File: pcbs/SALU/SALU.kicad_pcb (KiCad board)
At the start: 4 copper layers, 99 parts, among them J201 Conn_02x20_Odd_Even, U201 74HC245, U202 74HC245, U301 74HC138, U302 74HC138, U401 74HC245, U402 74HC86, U403 74HC08, U404 74HC283, U405 74HC283, U406 74HC245, U407 74HC245, U501 74HC00, U502 74HC00, U503 74HC245, U504 74HC245, U601 74HC245, U602 74HC245, U701 74HC08, U702 74HCT125, U703 74HC245, U704 74HC245

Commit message: More routing
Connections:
- U406 pad 11: /Incrementer-Decrementer/RESULT7 -> /Barrel Shifters/RESULT7
- U406 pad 12: /Incrementer-Decrementer/RESULT6 -> /Barrel Shifters/RESULT6
- U406 pad 13: /Incrementer-Decrementer/RESULT5 -> /Barrel Shifters/RESULT5
- U406 pad 14: /Incrementer-Decrementer/RESULT4 -> /Barrel Shifters/RESULT4
- U406 pad 15: /Incrementer-Decrementer/RESULT3 -> /Barrel Shifters/RESULT3
- U406 pad 16: /Incrementer-Decrementer/RESULT2 -> /Barrel Shifters/RESULT2
- U406 pad 17: /Incrementer-Decrementer/RESULT1 -> /Barrel Shifters/RESULT1
- U406 pad 18: /Incrementer-Decrementer/RESULT0 -> /Barrel Shifters/RESULT0
- U503 pad 11: /Incrementer-Decrementer/RESULT7 -> /Barrel Shifters/RESULT7
- U503 pad 12: /Incrementer-Decrementer/RESULT6 -> /Barrel Shifters/RESULT6
- U503 pad 13: /Incrementer-Decrementer/RESULT5 -> /Barrel Shifters/RESULT5
- U503 pad 14: /Incrementer-Decrementer/RESULT4 -> /Barrel Shifters/RESULT4
- U503 pad 15: /Incrementer-Decrementer/RESULT3 -> /Barrel Shifters/RESULT3
- U503 pad 16: /Incrementer-Decrementer/RESULT2 -> /Barrel Shifters/RESULT2
- U503 pad 17: /Incrementer-Decrementer/RESULT1 -> /Barrel Shifters/RESULT1
- U503 pad 18: /Incrementer-Decrementer/RESULT0 -> /Barrel Shifters/RESULT0
- U504 pad 11: /Incrementer-Decrementer/RESULT7 -> /Barrel Shifters/RESULT7
- U504 pad 12: /Incrementer-Decrementer/RESULT6 -> /Barrel Shifters/RESULT6
- U504 pad 13: /Incrementer-Decrementer/RESULT5 -> /Barrel Shifters/RESULT5
- U504 pad 14: /Incrementer-Decrementer/RESULT4 -> /Barrel Shifters/RESULT4
- U504 pad 15: /Incrementer-Decrementer/RESULT3 -> /Barrel Shifters/RESULT3
- U504 pad 16: /Incrementer-Decrementer/RESULT2 -> /Barrel Shifters/RESULT2
- U504 pad 17: /Incrementer-Decrementer/RESULT1 -> /Barrel Shifters/RESULT1
- U504 pad 18: /Incrementer-Decrementer/RESULT0 -> /Barrel Shifters/RESULT0
- U703 pad 11: /Shifters/RESULT7 -> /Barrel Shifters/RESULT7
- U703 pad 12: /Shifters/RESULT6 -> /Barrel Shifters/RESULT6
- U703 pad 13: /Shifters/RESULT5 -> /Barrel Shifters/RESULT5
- U703 pad 14: /Shifters/RESULT4 -> /Barrel Shifters/RESULT4
- U703 pad 15: /Shifters/RESULT3 -> /Barrel Shifters/RESULT3
- U703 pad 16: /Shifters/RESULT2 -> /Barrel Shifters/RESULT2
- U703 pad 17: /Shifters/RESULT1 -> /Barrel Shifters/RESULT1
- U703 pad 18: /Shifters/RESULT0 -> /Barrel Shifters/RESULT0
- U704 pad 11: /Shifters/RESULT7 -> /Barrel Shifters/RESULT7
- U704 pad 12: /Shifters/RESULT6 -> /Barrel Shifters/RESULT6
- U704 pad 13: /Shifters/RESULT5 -> /Barrel Shifters/RESULT5
- U704 pad 14: /Shifters/RESULT4 -> /Barrel Shifters/RESULT4
- U704 pad 15: /Shifters/RESULT3 -> /Barrel Shifters/RESULT3
- U704 pad 16: /Shifters/RESULT2 -> /Barrel Shifters/RESULT2
- U704 pad 17: /Shifters/RESULT1 -> /Barrel Shifters/RESULT1
- U704 pad 18: /Shifters/RESULT0 -> /Barrel Shifters/RESULT0
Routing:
- net /Barrel Shifters/RESULT6: track 0.00 -> 225.4 mm, vias 0 -> 9
- net /Barrel Shifters/RESULT7: track 0.00 -> 224.9 mm, vias 0 -> 9
- net /Barrel Shifters/RESULT5: track 0.00 -> 215.8 mm, vias 0 -> 9
- net /Barrel Shifters/RESULT4: track 0.00 -> 215.5 mm, vias 0 -> 9
- net /Barrel Shifters/RESULT3: track 0.00 -> 215.2 mm, vias 0 -> 9
- net /Barrel Shifters/RESULT2: track 0.00 -> 215.0 mm, vias 0 -> 9
- net /Barrel Shifters/RESULT1: track 0.00 -> 214.0 mm, vias 0 -> 9
- net /Barrel Shifters/RESULT0: track 0.00 -> 213.7 mm, vias 0 -> 9
- net /Incrementer-Decrementer/RESULT0: track 137.8 -> 0.00 mm, vias 4 -> 0
- net /Incrementer-Decrementer/RESULT1: track 135.0 -> 0.00 mm, vias 4 -> 0
- net /Incrementer-Decrementer/RESULT2: track 132.9 -> 0.00 mm, vias 4 -> 0
- net /Incrementer-Decrementer/RESULT6: track 131.2 -> 0.00 mm, vias 4 -> 0
- net /Incrementer-Decrementer/RESULT3: track 130.1 -> 0.00 mm, vias 4 -> 0
- net /Incrementer-Decrementer/RESULT7: track 127.6 -> 0.00 mm, vias 4 -> 0
- net /Incrementer-Decrementer/RESULT4: track 127.3 -> 0.00 mm, vias 4 -> 0
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
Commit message: Fiddling around with shifters
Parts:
- moved C703 22.2 mm to (138.4, 47.0)
- moved C704 20.4 mm to (138.4, 62.2)
- moved C702 11.4 mm to (148.6, 22.9)
- moved U702 11.4 mm to (141.0, 26.7)
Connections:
- U701 pad 1: /Shifters/~{LSHIFT0} -> GND
- U701 pad 10: GND -> /Shifters/~{LSHIFT1}
- U701 pad 2: /Shifters/~{LSHIFT1} -> GND
- U701 pad 3: Net-(U701-Pad3) -> unconnected-(U701-Pad3)
- U701 pad 8: unconnected-(U701-Pad8) -> Net-(U703-Pad19)
- U701 pad 9: GND -> /Shifters/~{LSHIFT0}
- U702 pad 1: /Shifters/~{LSHIFT0} -> /Shifters/~{RSHIFT1}
- U702 pad 10: /Shifters/~{RSHIFT0} -> /Shifters/~{LSHIFT0}
- U702 pad 12: /Barrel Shifters/A0 -> /Barrel Shifters/A7
- U702 pad 13: /Shifters/~{RSHIFT1} -> /Shifters/~{LSHIFT1}
- U702 pad 2: /Barrel Shifters/A7 -> /Barrel Shifters/A0
- U702 pad 4: /Shifters/~{LSHIFT1} -> /Shifters/~{RSHIFT0}
- U702 pad 5: /Barrel Shifters/A7 -> /Barrel Shifters/A0
- U702 pad 9: /Barrel Shifters/A0 -> /Barrel Shifters/A7
- U703 pad 19: Net-(U701-Pad3) -> Net-(U703-Pad19)
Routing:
- net /Shifters/~{RSHIFT0}: track 0.00 -> 78.7 mm, vias 0 -> 2
- net /Shifters/~{LSHIFT0}: track 0.00 -> 72.4 mm, vias 0 -> 2
- net /Barrel Shifters/A7: track 253.8 -> 322.9 mm
- net Net-(U701-Pad6): track 0.00 -> 50.1 mm, vias 0 -> 2
- net /Barrel Shifters/A0: track 287.7 -> 325.9 mm
- net /Shifters/~{RSHIFT1}: track 0.00 -> 35.5 mm
- net /Shifters/FLAG: track 0.00 -> 31.6 mm
- net /Shifters/~{LSHIFT1}: track 0.00 -> 31.1 mm, vias 0 -> 1
- net Net-(U703-Pad19): track 0.00 -> 2.67 mm, vias 0 -> 1

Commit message: Working on output stage
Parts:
- added C801: 100n, Capacitor_SMD:C_0603_1608Metric, F.Cu at (174.0, 35.6)
- added C802: 100n, Capacitor_SMD:C_0603_1608Metric, F.Cu at (174.0, 58.4)
- added C803: 100n, Capacitor_SMD:C_0603_1608Metric, F.Cu at (157.5, 66.3)
- added C804: 100n, Capacitor_SMD:C_0603_1608Metric, F.Cu at (174.0, 82.5)
- added D801: GREEN, LED_SMD:LED_0603_1608Metric, F.Cu at (159.0, 85.1)
- added D802: GREEN, LED_SMD:LED_0603_1608Metric, F.Cu at (159.0, 87.6)
- added D803: GREEN, LED_SMD:LED_0603_1608Metric, F.Cu at (159.0, 90.2)
- added D804: GREEN, LED_SMD:LED_0603_1608Metric, F.Cu at (159.0, 92.7)
- added D805: GREEN, LED_SMD:LED_0603_1608Metric, F.Cu at (159.0, 95.2)
- added D806: GREEN, LED_SMD:LED_0603_1608Metric, F.Cu at (159.0, 97.8)
- added D807: GREEN, LED_SMD:LED_0603_1608Metric, F.Cu at (159.0, 100.3)
- added D808: GREEN, LED_SMD:LED_0603_1608Metric, F.Cu at (159.0, 102.9)
- added R801: 220k, Resistor_SMD:R_0603_1608Metric, F.Cu at (135.9, 81.1)
- added R802: 220k, Resistor_SMD:R_0603_1608Metric, F.Cu at (137.2, 77.3)
- added R803: 220k, Resistor_SMD:R_0603_1608Metric, F.Cu at (138.4, 81.1)
- added R804: 220k, Resistor_SMD:R_0603_1608Metric, F.Cu at (139.7, 77.3)
- added R805: 220k, Resistor_SMD:R_0603_1608Metric, F.Cu at (141.0, 81.1)
- added R806: 220k, Resistor_SMD:R_0603_1608Metric, F.Cu at (142.2, 77.3)
- added R807: 220k, Resistor_SMD:R_0603_1608Metric, F.Cu at (143.5, 81.1)
- added R808: 220k, Resistor_SMD:R_0603_1608Metric, F.Cu at (144.8, 77.3)
- added R809: 4k7, Resistor_SMD:R_0603_1608Metric, F.Cu at (155.2, 85.1)
- added R810: 4k7, Resistor_SMD:R_0603_1608Metric, F.Cu at (155.2, 87.6)
- added R811: 4k7, Resistor_SMD:R_0603_1608Metric, F.Cu at (155.2, 90.2)
- added R812: 4k7, Resistor_SMD:R_0603_1608Metric, F.Cu at (155.2, 92.7)
- added R813: 4k7, Resistor_SMD:R_0603_1608Metric, F.Cu at (155.2, 95.2)
- added R814: 4k7, Resistor_SMD:R_0603_1608Metric, F.Cu at (155.2, 97.8)
- added R815: 4k7, Resistor_SMD:R_0603_1608Metric, F.Cu at (155.2, 100.3)
- added R816: 4k7, Resistor_SMD:R_0603_1608Metric, F.Cu at (155.2, 102.9)
- added R817: 10k, Resistor_THT:R_Axial_DIN0207_L6.3mm_D2.5mm_P7.62mm_Horizontal, F.Cu at (157.5, 38.1)
- added U801: 74HC74, Package_DIP:DIP-14_W7.62mm_Socket, F.Cu at (162.6, 35.6)
- added U802: 74HC32, Package_DIP:DIP-14_W7.62mm_Socket, F.Cu at (162.6, 58.4)
- added U803: 74HC14, Package_SO:SOIC-14_3.9x8.7mm_P1.27mm, F.Cu at (154.9, 72.6)
- added U804: 74HCT574, Package_DIP:DIP-20_W7.62mm_Socket, F.Cu at (162.6, 82.5)
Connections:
- U702 pad 11: /Shifters/FLAG -> /Incrementer-Decrementer/FLAG
- U702 pad 3: /Shifters/FLAG -> /Incrementer-Decrementer/FLAG
- U702 pad 6: /Shifters/FLAG -> /Incrementer-Decrementer/FLAG
- U702 pad 8: /Shifters/FLAG -> /Incrementer-Decrementer/FLAG
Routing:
- net /Incrementer-Decrementer/FLAG: track 0.00 -> 94.4 mm, vias 0 -> 1
- net /Output Stage/EXECUTE: track 0.00 -> 80.4 mm
- net /Barrel Shifters/RESULT5: track 215.8 -> 262.9 mm, vias 9 -> 10
- net /Barrel Shifters/RESULT7: track 224.9 -> 267.7 mm, vias 9 -> 10
- net /Barrel Shifters/RESULT3: track 215.2 -> 257.5 mm, vias 9 -> 10
- net /Barrel Shifters/RESULT4: track 215.5 -> 256.5 mm, vias 9 -> 10
- net /Barrel Shifters/RESULT1: track 214.0 -> 252.5 mm, vias 9 -> 10
- net /Barrel Shifters/RESULT6: track 225.4 -> 261.9 mm, vias 9 -> 10
- net /Barrel Shifters/RESULT2: track 215.0 -> 251.2 mm, vias 9 -> 10
- net /Barrel Shifters/RESULT0: track 213.7 -> 246.8 mm, vias 9 -> 10
- net /Shifters/FLAG: track 31.6 -> 0.00 mm
- net /Output Stage/~{OE}: track 0.00 -> 16.0 mm
- net Net-(U802-Pad6): track 0.00 -> 5.88 mm
- net Net-(U802-Pad3): track 0.00 -> 2.54 mm
- net Net-(D807-Pad1): track 0.00 -> 2.20 mm
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
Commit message: Routing
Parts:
- moved J201 14.2 mm to (38.1, 64.8)
- moved R309 1.52 mm to (73.7, 132.1)
- moved D305 1.27 mm to (69.8, 142.2)
- moved D307 1.27 mm to (69.8, 137.2)
- moved D308 1.27 mm to (69.8, 139.7)
- moved D309 1.27 mm to (69.8, 127.0)
- moved D310 1.27 mm to (69.8, 129.5)
- moved D311 1.27 mm to (69.8, 132.1)
- moved D312 1.27 mm to (69.8, 134.6)
- moved D313 1.27 mm to (69.8, 168.9)
- moved D315 1.27 mm to (69.8, 153.7)
- moved D316 1.27 mm to (69.8, 156.2)
- moved D317 1.27 mm to (69.8, 158.8)
- moved D318 1.27 mm to (69.8, 161.3)
- moved D319 1.27 mm to (69.8, 163.8)
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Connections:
- J201 pad 19: /Connector/DALUFLAG -> /Connector/SALUFLAG
- U401 pad 19: /Incrementer-Decrementer/~{INC} -> /Instruction Decoder/~{INC}
- U402 pad 4: /Incrementer-Decrementer/~{INC} -> /Instruction Decoder/~{INC}
- U403 pad 1: /Incrementer-Decrementer/~{INC} -> /Instruction Decoder/~{INC}
- U403 pad 2: /Incrementer-Decrementer/~{DEC} -> /Instruction Decoder/~{DEC}
- U404 pad 7: /Incrementer-Decrementer/~{INC} -> /Instruction Decoder/~{INC}
- U503 pad 19: /Not-Copy/~{NOT} -> /Instruction Decoder/~{NOT}
- U504 pad 19: /Not-Copy/~{COPY} -> /Instruction Decoder/~{COPY}
- U601 pad 19: /Barrel Shifters/~{LBARREL} -> /Instruction Decoder/~{LBARREL}
- U602 pad 19: /Barrel Shifters/~{RBARREL} -> /Instruction Decoder/~{RBARREL}
- U701 pad 10: /Shifters/~{LSHIFT1} -> /Instruction Decoder/~{LSHIFT1}
- U701 pad 4: /Shifters/~{RSHIFT0} -> /Instruction Decoder/~{RSHIFT0}
- U701 pad 5: /Shifters/~{RSHIFT1} -> /Instruction Decoder/~{RSHIFT1}
- U701 pad 9: /Shifters/~{LSHIFT0} -> /Instruction Decoder/~{LSHIFT0}
- U702 pad 1: /Shifters/~{RSHIFT1} -> /Instruction Decoder/~{RSHIFT1}
- U702 pad 10: /Shifters/~{LSHIFT0} -> /Instruction Decoder/~{LSHIFT0}
- U702 pad 13: /Shifters/~{LSHIFT1} -> /Instruction Decoder/~{LSHIFT1}
- U702 pad 4: /Shifters/~{RSHIFT0} -> /Instruction Decoder/~{RSHIFT0}
- U703 pad 2: /Shifters/~{LSHIFT0} -> /Instruction Decoder/~{LSHIFT0}
- U704 pad 9: /Shifters/~{RSHIFT0} -> /Instruction Decoder/~{RSHIFT0}
- U801 pad 5: /Output Stage/SALUFLAG -> /Connector/SALUFLAG
- U804 pad 12: /Output Stage/C7 -> /Connector/C7
- U804 pad 13: /Output Stage/C6 -> /Connector/C6
- U804 pad 14: /Output Stage/C5 -> /Connector/C5
- U804 pad 15: /Output Stage/C4 -> /Connector/C4
- U804 pad 16: /Output Stage/C3 -> /Connector/C3
- U804 pad 17: /Output Stage/C2 -> /Connector/C2
- U804 pad 18: /Output Stage/C1 -> /Connector/C1
- U804 pad 19: /Output Stage/C0 -> /Connector/C0
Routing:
- net /Connector/C7: track 0.00 -> 196.6 mm
- net /Connector/C6: track 0.00 -> 192.5 mm
- net /Connector/C5: track 0.00 -> 188.4 mm
- net /Connector/C4: track 0.00 -> 184.4 mm
- net /Instruction Decoder/~{LSHIFT1}: track 0.00 -> 182.8 mm, vias 0 -> 1
- net /Connector/C3: track 0.00 -> 180.3 mm
- net /Instruction Decoder/~{RSHIFT0}: track 0.00 -> 178.0 mm, vias 0 -> 2
- net /Connector/C2: track 0.00 -> 176.2 mm
- net /Connector/C1: track 0.00 -> 172.2 mm
- net /Instruction Decoder/~{LSHIFT0}: track 0.00 -> 171.2 mm, vias 0 -> 4
- net /Connector/C0: track 0.00 -> 168.1 mm
- net /Instruction Decoder/~{RSHIFT1}: track 0.00 -> 146.0 mm, vias 0 -> 1
- net /Connector/SALUFLAG: track 0.00 -> 145.7 mm
- net /Instruction Decoder/~{DEC}: track 0.00 -> 114.8 mm
- net /Instruction Decoder/~{INC}: track 0.00 -> 99.9 mm, vias 0 -> 2
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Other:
- board text added: "RGE2023"

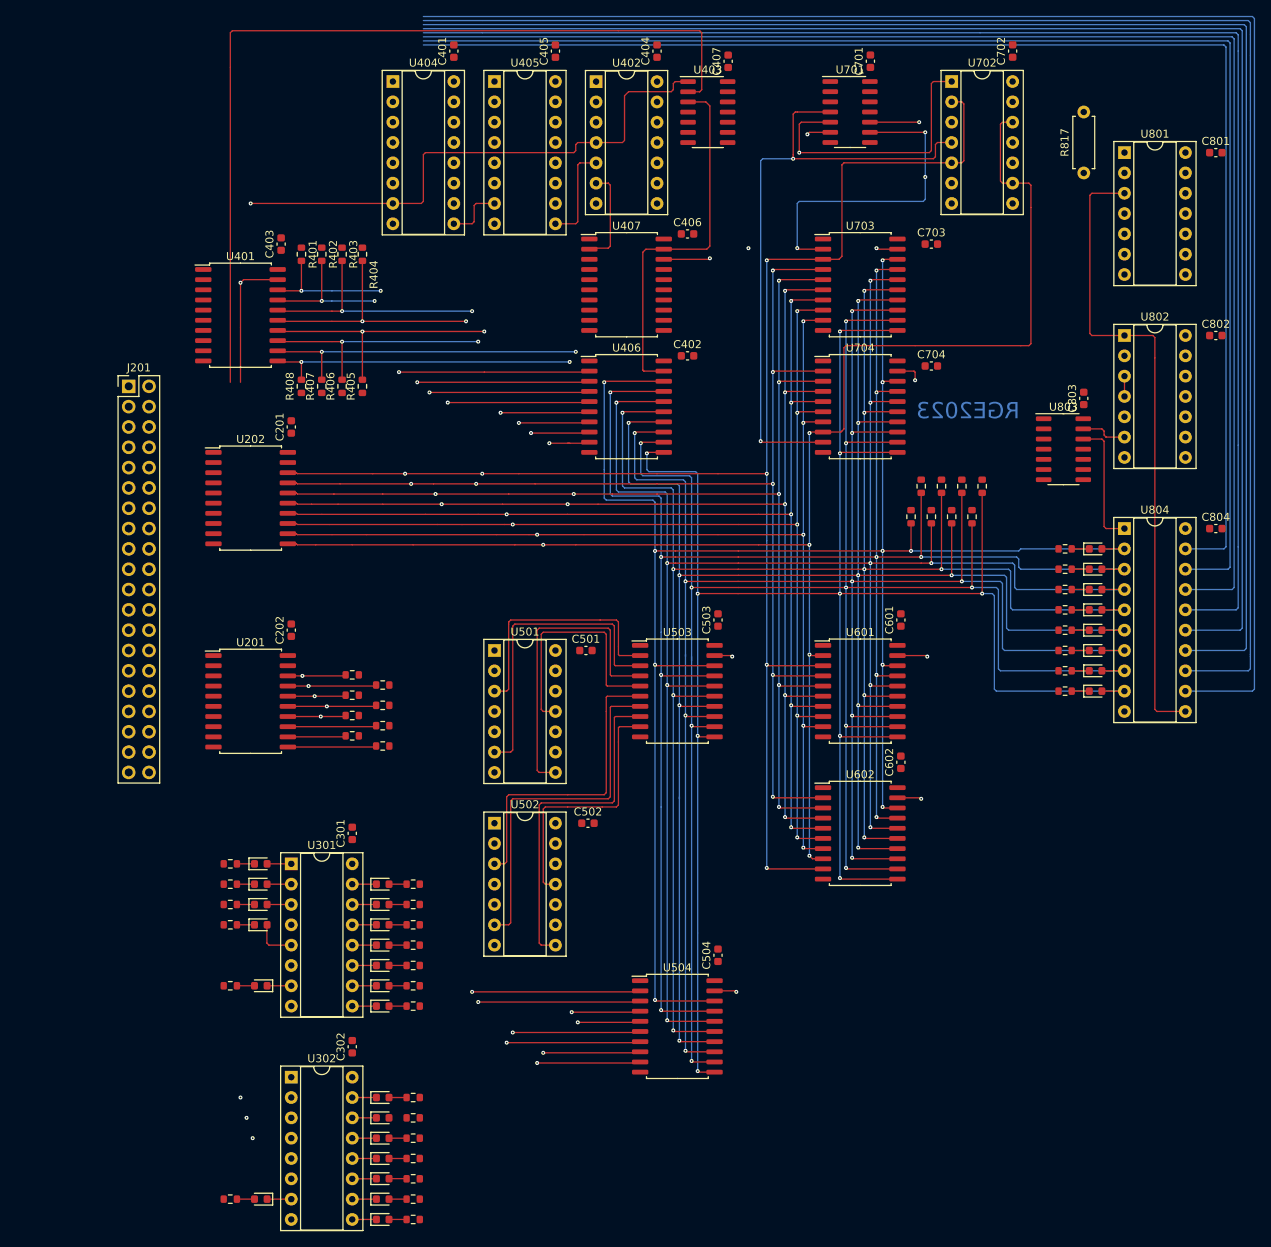
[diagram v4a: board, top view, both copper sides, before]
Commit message: Rethink position of second decoder
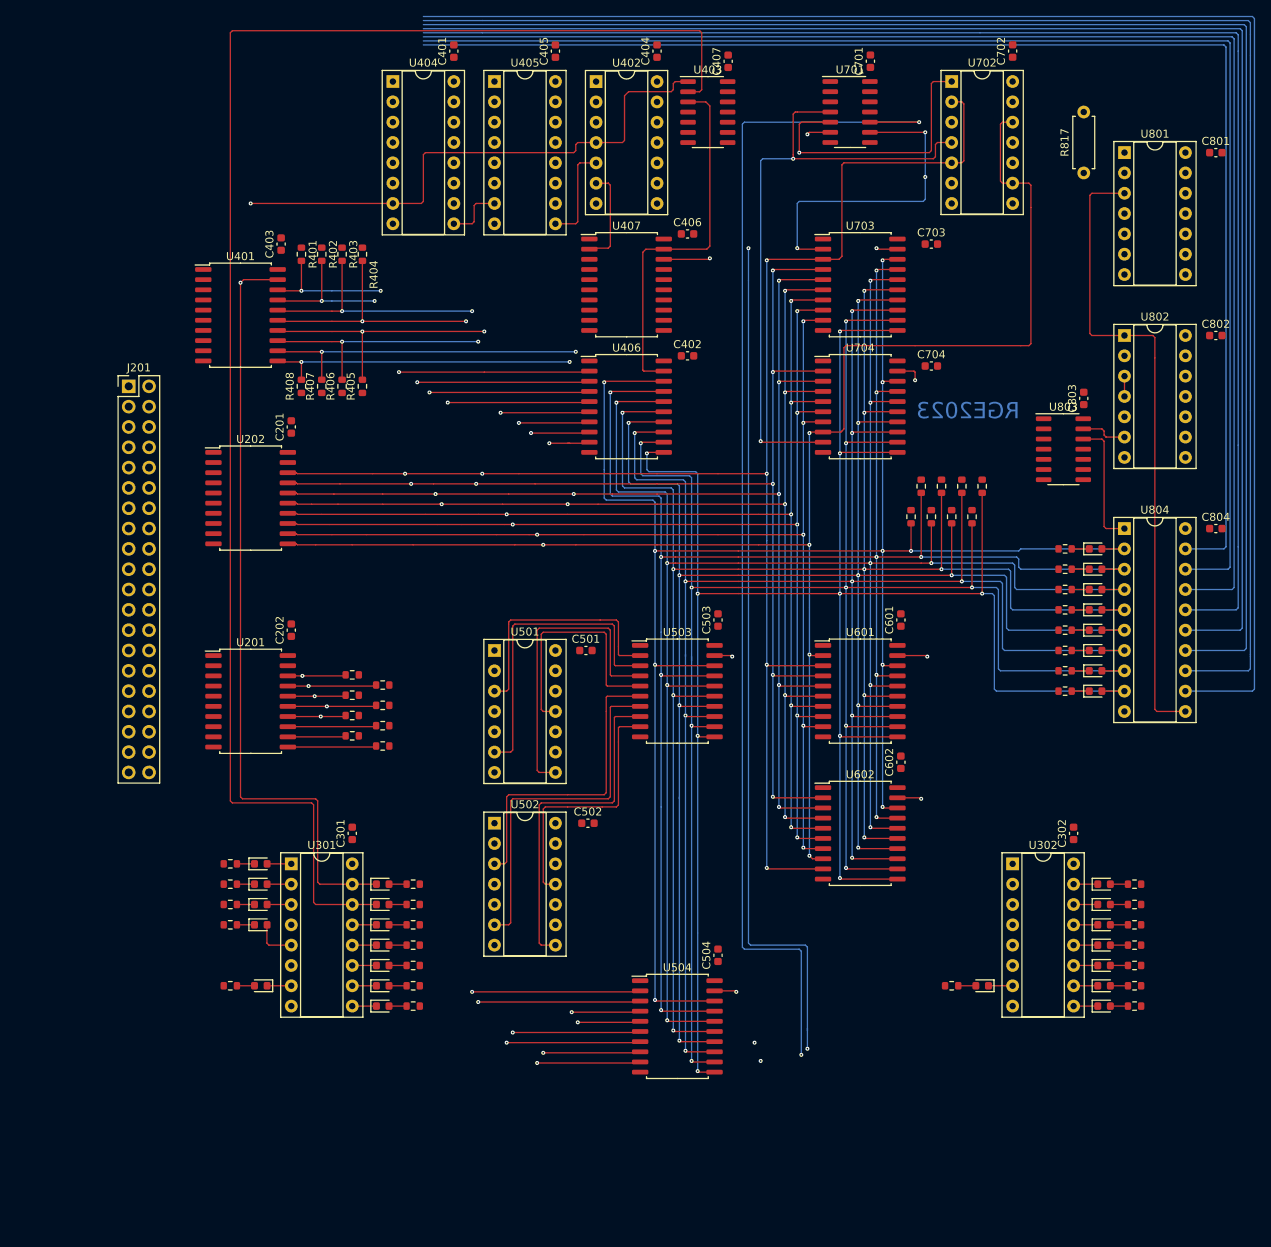
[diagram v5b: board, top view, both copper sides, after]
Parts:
- moved D316 94.0 mm to (160.0, 129.5)
- moved D320 94.0 mm to (160.0, 139.7)
- moved R316 94.0 mm to (163.8, 129.5)
- moved R317 94.0 mm to (163.8, 137.2)
- moved R318 94.0 mm to (163.8, 139.7)
- moved D314 94.0 mm to (144.8, 139.7)
- moved R314 94.0 mm to (141.0, 139.7)
- moved U302 94.0 mm to (148.6, 124.5)
- moved D313 94.0 mm to (160.0, 142.2)
- moved D315 94.0 mm to (160.0, 127.0)
- moved D317 94.0 mm to (160.0, 132.1)
- moved D318 94.0 mm to (160.0, 134.6)
- moved R313 94.0 mm to (163.8, 142.2)
- moved R315 94.0 mm to (163.8, 127.0)
- moved R319 94.0 mm to (163.8, 132.1)
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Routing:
- net /Connector/Control.I0: track 65.2 -> 209.1 mm
- net /Connector/Control.I1: track 80.3 -> 206.8 mm, vias 2 -> 1
- net /Connector/Control.I2: track 77.0 -> 196.9 mm, vias 2 -> 1
- net /Connector/Control.~{SELECT}: track 73.2 -> 186.5 mm, vias 2 -> 1
- net /Connector/Control.I3: track 87.9 -> 189.7 mm
- net /Instruction Decoder/~{DEC}: track 114.8 -> 194.9 mm
- net /Instruction Decoder/~{INC}: track 99.9 -> 176.1 mm
- net /Instruction Decoder/~{LSHIFT0}: track 171.2 -> 232.4 mm, vias 4 -> 5
- net /Instruction Decoder/~{NOT}: track 76.6 -> 137.5 mm
- net /Instruction Decoder/~{COPY}: track 32.3 -> 89.2 mm
- net /Instruction Decoder/~{RSHIFT1}: track 146.0 -> 197.5 mm, vias 1 -> 2
- net /Instruction Decoder/~{LSHIFT1}: track 182.8 -> 222.1 mm, vias 1 -> 2
- net /Instruction Decoder/~{RSHIFT0}: track 178.0 -> 205.1 mm, vias 2 -> 3
- net /Instruction Decoder/~{RBARREL}: track 26.9 -> 38.0 mm
- net /Instruction Decoder/~{LBARREL}: track 45.4 -> 53.2 mm
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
